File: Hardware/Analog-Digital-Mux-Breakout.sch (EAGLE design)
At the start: 11 parts, among them U1 MUX-74HC4067

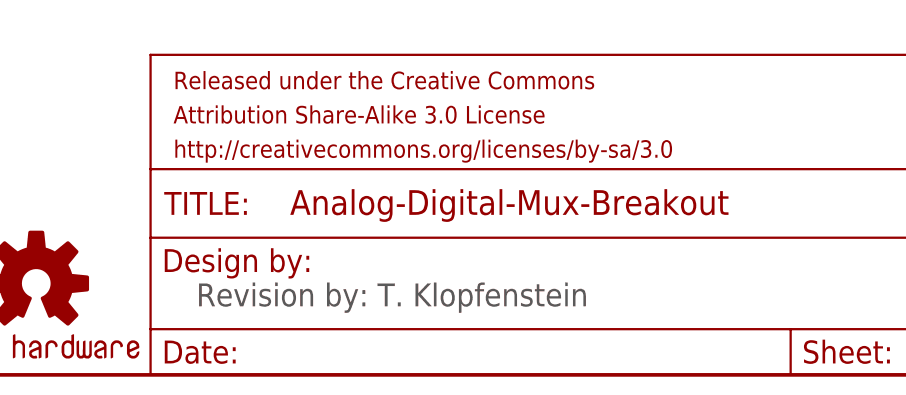
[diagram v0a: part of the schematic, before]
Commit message: Updated Revision to symbol
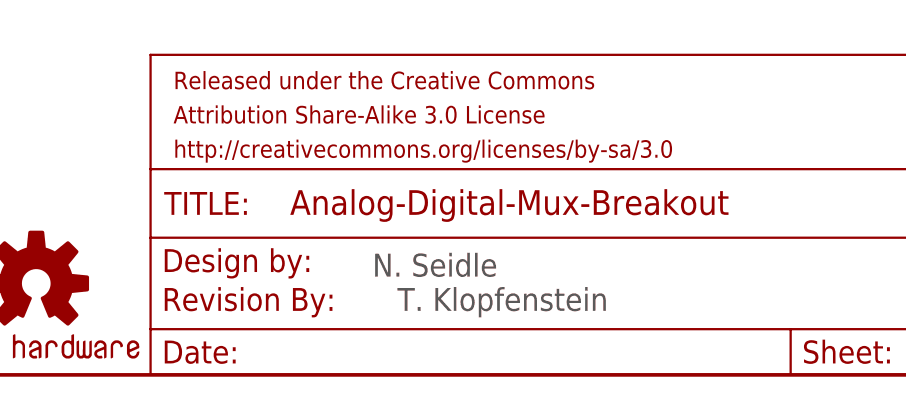
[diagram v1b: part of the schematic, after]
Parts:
- added U$2: REVISION, SparkFun-Aesthetics:REVISION
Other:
- note added: "N. Seidle"
- note added: "T. Klopfenstein"
- note removed: "Revision by: T. Klopfenstein"
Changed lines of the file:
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@@
 <part name="STANDOFF2" library="SparkFun-Electromechanical" deviceset="STAND-OFF" device=""/>
 <part name="LOGO2" library="SparkFun-Aesthetics" deviceset="LOGO-SFE" device="SK"/>
+<part name="U$2" library="SparkFun-Aesthetics" deviceset="REVISION" device=""/>
 </parts>
 <sheets>
@@
 <plain>
 <text x="238.76" y="7.62" size="2.54" layer="97">v11</text>
-<text x="152.4" y="7.62" size="2.54" layer="97">Revision by: T. Klopfenstein</text>
+<text x="171.958" y="10.922" size="2.54" layer="97">N. Seidle</text>
+<text x="174.752" y="7.112" size="2.54" layer="97">T. Klopfenstein</text>
 </plain>
 <instances>
@@
 <instance part="STANDOFF2" gate="G$1" x="241.3" y="25.4"/>
 <instance part="LOGO2" gate="G$1" x="241.3" y="30.48"/>
+<instance part="U$2" gate="G$1" x="148.59" y="7.112"/>
 </instances>
 <busses>
